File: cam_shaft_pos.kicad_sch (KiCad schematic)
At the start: 2 parts, among them J11 Conn_01x90_3Row_Socket, U47 Cam Shaft

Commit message: external loops
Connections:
- net B86: no longer names the net of J11.87 (B87)
- net B86: no longer U47.3 (V_{CC})
- new net PWR_12V: U47.3 (V_{CC})
- no-connect marks 87 -> 88

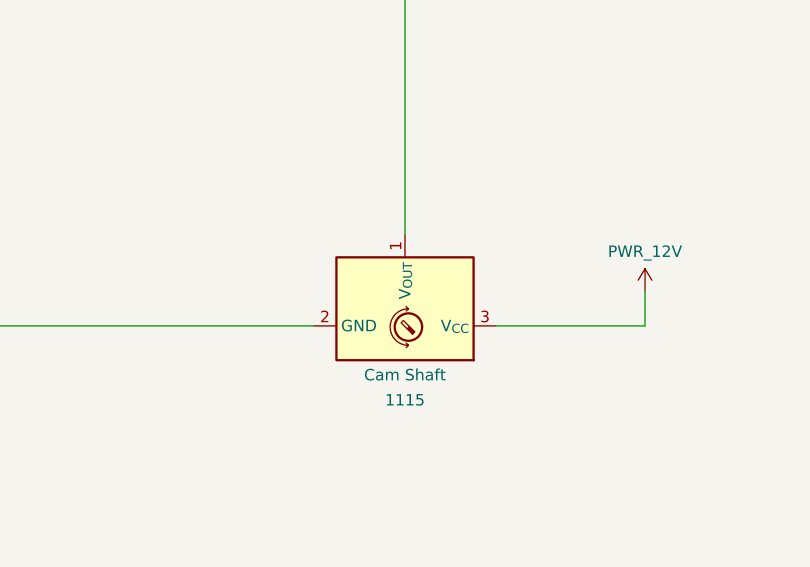
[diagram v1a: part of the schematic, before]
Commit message: air conditioner updated
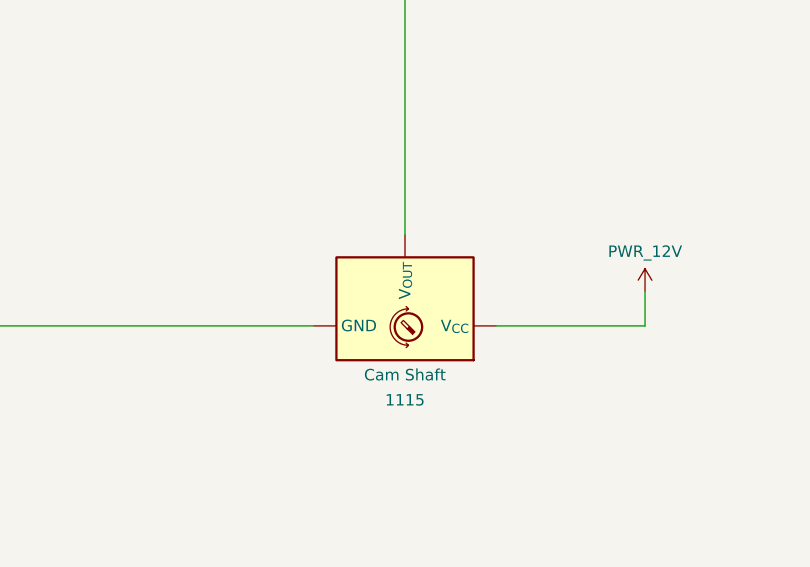
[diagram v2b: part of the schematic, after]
